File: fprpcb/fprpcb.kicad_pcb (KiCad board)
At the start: 2 copper layers, 119.8 x 90.3 mm, 49 parts, among them J1 Conn_02x04_Odd_Even, J2 Conn_01x02, J3 Conn_01x03, J4 Conn_01x03, J5 Conn_01x03, J6 Conn_01x03, J7 Conn_01x06, J8 Conn_01x04, SW1 Conn_01x02_Pin, SW2 Conn_01x02_Pin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

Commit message: updated fprpcb
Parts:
- moved U4 19.7 mm to (62.2, 70.8), turned to 0 degrees
- moved R14 16.1 mm to (94.2, 68.2)
- moved J2 13.6 mm to (96.6, 83.4), turned to 0 degrees
- moved R15 5.37 mm to (94.3, 74.9)
- moved J5 5.35 mm to (156.5, 100.6), turned to -90 degrees
- moved R5 1.50 mm to (119.2, 76.8)
- moved R17 1.18 mm to (107.3, 76.8)
- moved SW3 0.54 mm to (132.6, 68.7)
- moved J4 0.48 mm to (170.0, 100.8)
- moved J7 0.41 mm to (107.9, 142.3)
- moved R9 0.35 mm to (131.3, 76.8)
- moved SW6 0.31 mm to (108.6, 68.7)
- moved C8 0.30 mm to (109.2, 83.4)
- moved C3 0.20 mm to (133.1, 83.4)
- moved R16 0.18 mm to (107.3, 73.6)
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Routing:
- net +3.3V: track 274.7 -> 347.9 mm
- net GND: track 456.6 -> 503.8 mm, vias 0 -> 1
- net /SW3: track 118.5 -> 158.1 mm, vias 1 -> 6
- net /SW1: track 74.0 -> 100.1 mm, vias 1 -> 0
- net /GP28_ADC2: track 41.5 -> 64.8 mm
- net /B-: track 30.2 -> 10.8 mm
- net GNDA: track 90.6 -> 107.3 mm
- net /I2C0_SDA: track 80.4 -> 64.0 mm, vias 0 -> 1
- net VDDA: track 101.9 -> 117.8 mm, vias 0 -> 2
- net /SPI0_MISO: track 61.2 -> 46.0 mm
- net /GP27_ADC1: track 77.4 -> 91.3 mm, vias 0 -> 2
- net VBUS: track 99.7 -> 112.1 mm, vias 0 -> 2
- net /SPI0_MOSI: track 58.1 -> 46.0 mm
- net /GP26_ADC0: track 88.0 -> 98.7 mm, vias 0 -> 3
- net /B+: track 21.2 -> 12.9 mm
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
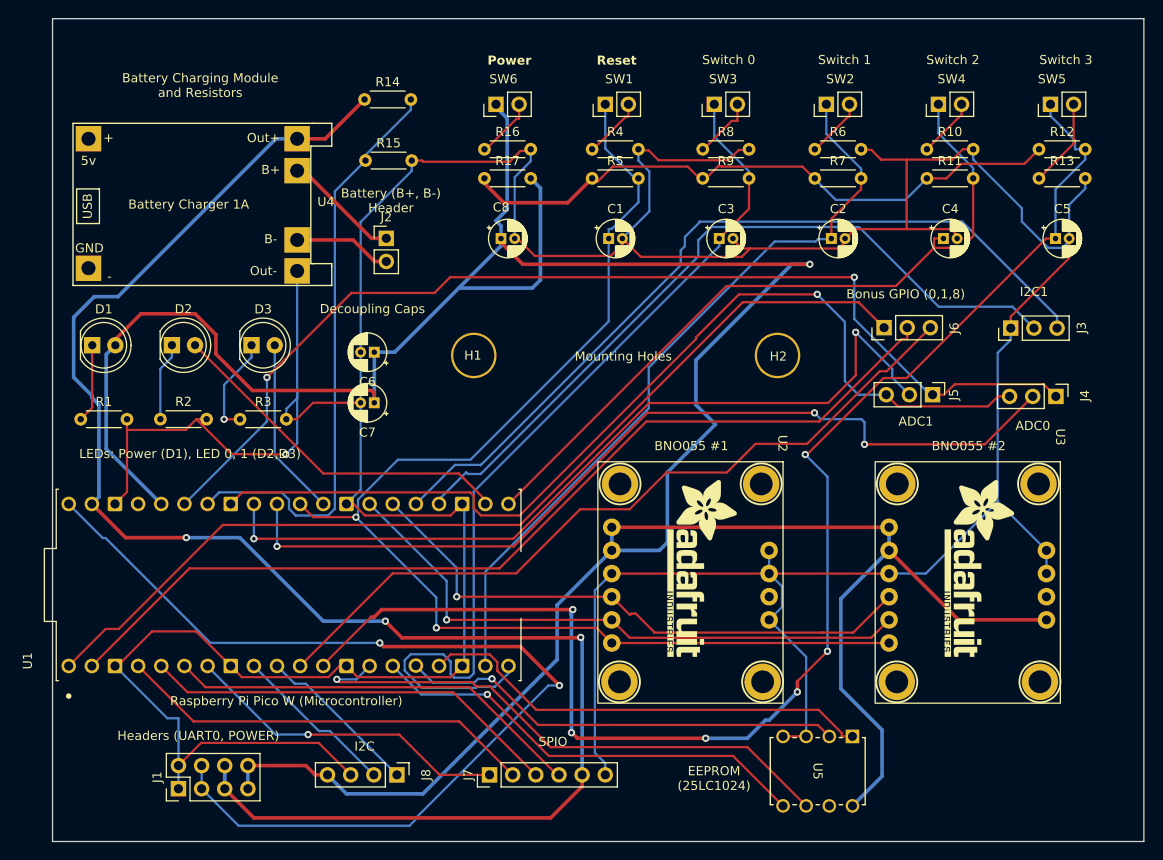
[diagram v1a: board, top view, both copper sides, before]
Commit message: fixed power switch issue where ghost components were showing up on the board
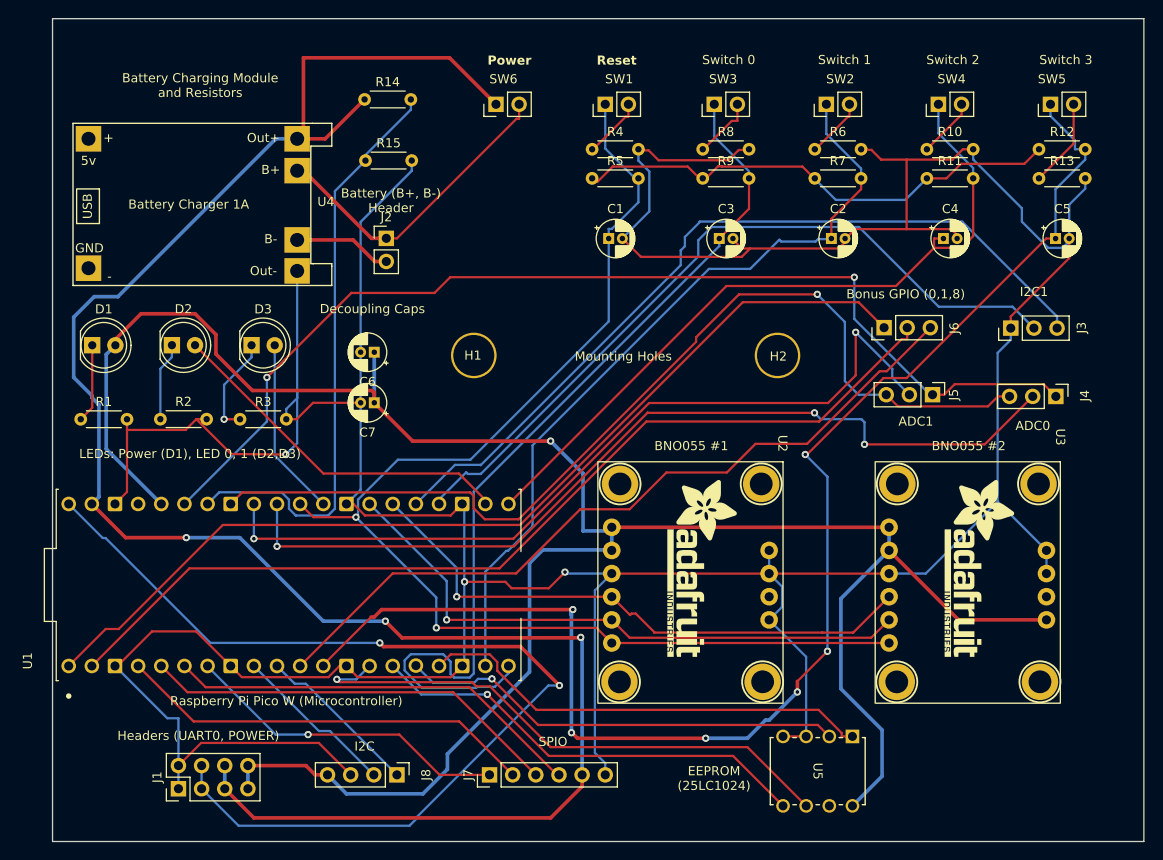
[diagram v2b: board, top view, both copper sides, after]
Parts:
- removed C8: 100nF, Capacitor_THT:CP_Radial_D4.0mm_P1.50mm
- removed R16: 100, Resistor_THT:R_Axial_DIN0204_L3.6mm_D1.6mm_P5.08mm_Horizontal
- removed R17: 10k, Resistor_THT:R_Axial_DIN0204_L3.6mm_D1.6mm_P5.08mm_Horizontal
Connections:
- SW6 pad 1: +3.3V -> +5V
- SW6 pad 2: Net-(SW6-Pin_2) -> /B+
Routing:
- net +3.3V: track 347.9 -> 250.0 mm
- net +5V: track 184.5 -> 216.9 mm
- net /B+: track 12.9 -> 34.1 mm
- net GND: track 503.8 -> 483.6 mm, vias 1 -> 3
- net +3V3: track 69.3 -> 54.9 mm
- net Net-(SW6-Pin_2): track 6.54 -> 0.00 mm
- net /SW0: track 83.7 -> 86.5 mm
- net GNDA: track 107.3 -> 107.9 mm

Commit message: fprpcb (again and fr this time 💀)
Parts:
- moved J6 5.34 mm to (156.5, 93.2), turned to -90 degrees
- moved R13 3.34 mm to (168.6, 73.5)
- moved R12 3.08 mm to (168.6, 76.7)
- moved U4 2.06 mm to (60.1, 71.0)
- moved J5 0.26 mm to (156.3, 100.6)
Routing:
- net /GP0_UART0_TX: track 107.2 -> 187.4 mm
- net GND: track 483.6 -> 502.1 mm
- net /B+: track 34.1 -> 42.0 mm
- net Net-(SW5-Pin_2): track 9.70 -> 6.23 mm
- net /GP8_UART1_TX: track 84.5 -> 88.0 mm, vias 0 -> 2
- net /B-: track 10.8 -> 13.1 mm
- net /SW3: track 158.1 -> 159.2 mm
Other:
- board text added: "InSight FPR PCB SDP 2024 Team 16 Anvitha, Tyler, Ivy, Khush Prof. McLaughlin"

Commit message: fprpcb
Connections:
- J1 pad 5: +5V -> VSYS
- J1 pad 6: +5V -> VSYS
- J7 pad 5: +5V -> VSYS
- R14 pad 1: +5V -> VSYS
- SW6 pad 1: +5V -> VSYS
- SW6 pad 2: /B+ -> VSYS
- U1 pad 39: +5V -> VSYS
- U4 pad 1: +5V -> VSYS
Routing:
- net VSYS: track 0.00 -> 320.7 mm, vias 0 -> 6
- net +5V: track 217.1 -> 0.00 mm, vias 3 -> 0
- net /B+: track 42.0 -> 20.5 mm
- net GND: track 502.1 -> 508.4 mm

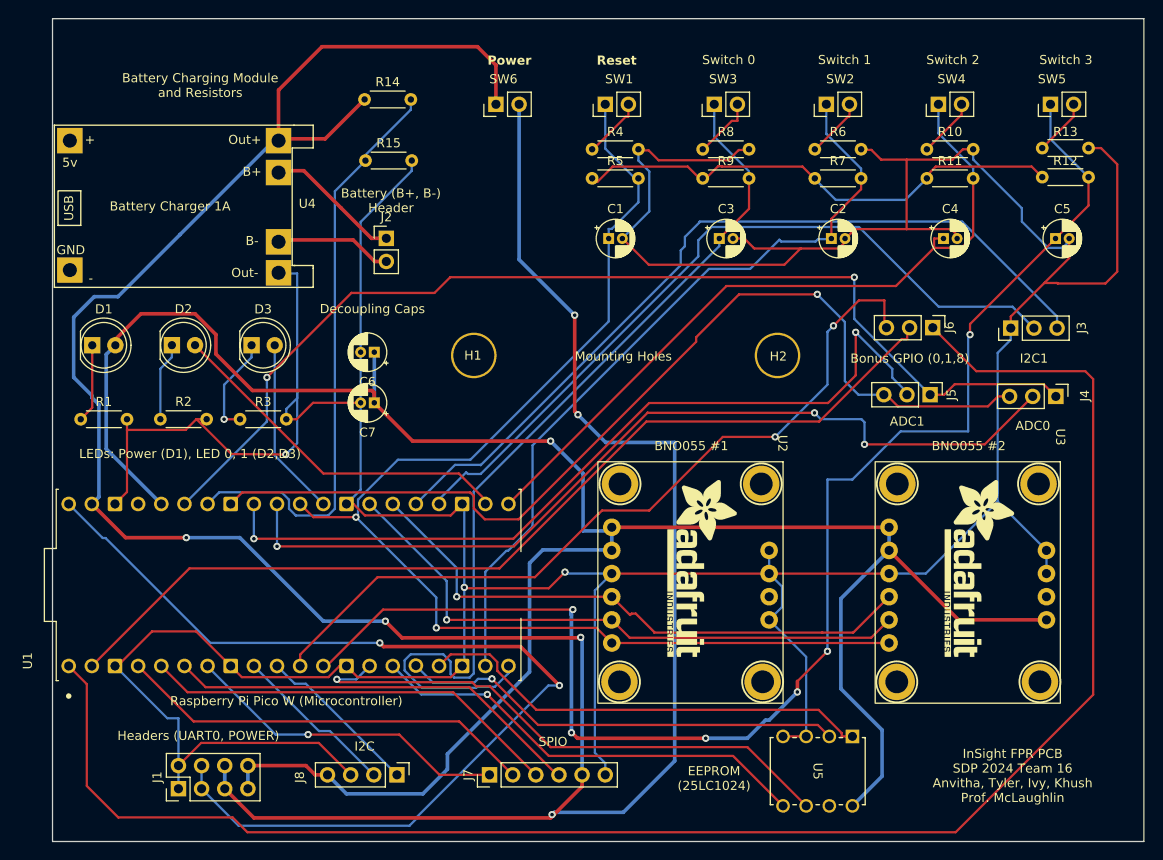
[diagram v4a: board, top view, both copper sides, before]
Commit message: Revert "fprpcb"
This reverts commit a24959e1a84143555ed98c59d3b6709d6d6878c6.
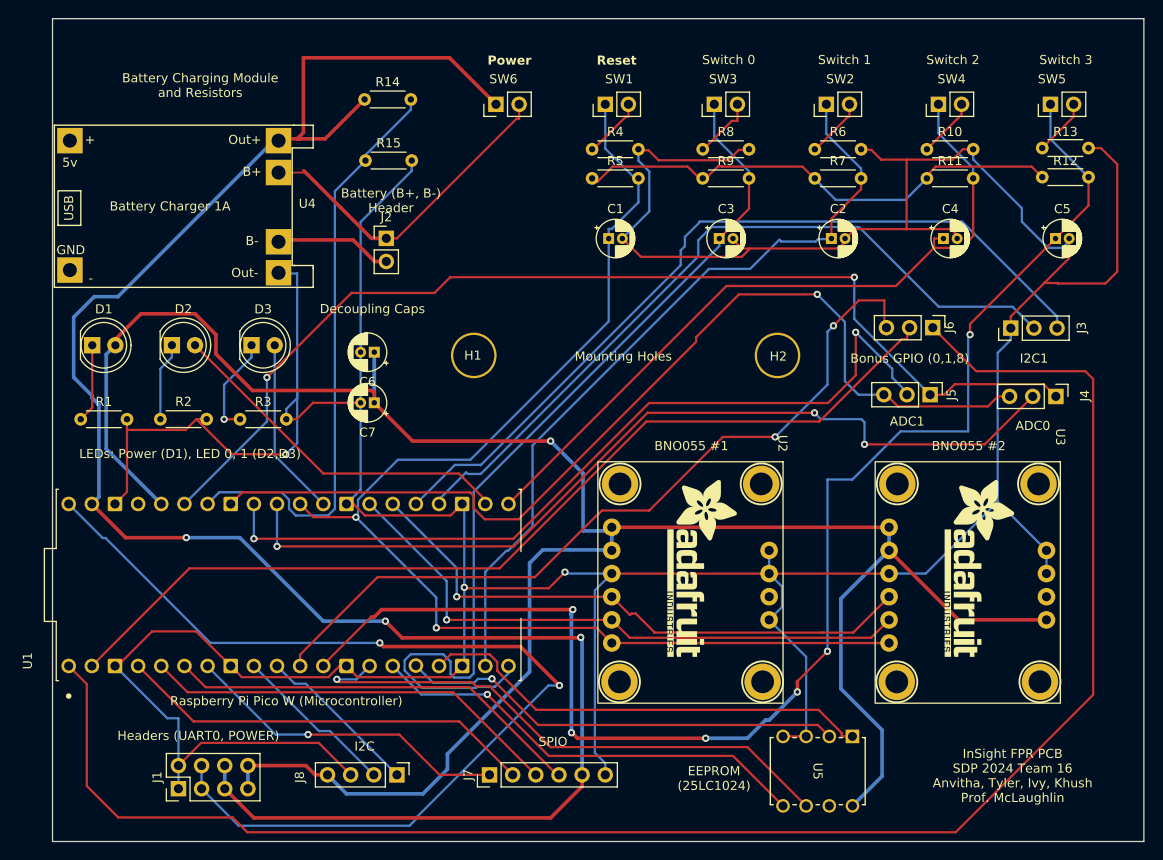
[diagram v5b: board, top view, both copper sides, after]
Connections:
- J1 pad 5: VSYS -> +5V
- J1 pad 6: VSYS -> +5V
- J7 pad 5: VSYS -> +5V
- R14 pad 1: VSYS -> +5V
- SW6 pad 1: VSYS -> +5V
- SW6 pad 2: VSYS -> /B+
- U1 pad 39: VSYS -> +5V
- U4 pad 1: VSYS -> +5V
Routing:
- net VSYS: track 320.7 -> 0.00 mm, vias 6 -> 0
- net +5V: track 0.00 -> 217.1 mm, vias 0 -> 3
- net /B+: track 20.5 -> 42.0 mm
- net GND: track 508.4 -> 502.1 mm

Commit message: update repo with true PCB that has all the fixed ones because the old one only updated the schematic
💀💀💀💀💀💀💀
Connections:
- J1 pad 5: +5V -> VSYS
- J1 pad 6: +5V -> VSYS
- J7 pad 5: +5V -> VSYS
- R14 pad 1: +5V -> VSYS
- SW6 pad 1: +5V -> VSYS
- SW6 pad 2: /B+ -> VSYS
- U1 pad 39: +5V -> VSYS
- U4 pad 1: +5V -> VSYS
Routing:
- net VSYS: track 0.00 -> 318.0 mm, vias 0 -> 6
- net +5V: track 217.1 -> 0.00 mm, vias 3 -> 0
- net /B+: track 42.0 -> 14.8 mm
